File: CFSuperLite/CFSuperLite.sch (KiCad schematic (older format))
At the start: 23 parts, among them J1 IDE_CONNECTOR, J2 CF Adapter Power, J3 Bus_ISA_8bit, SW1 Options, U1 BIOS FLASH, U2 74HCT245, U3 ATF/GAL16V8x-15, U4 DS1315, Y1 32.768 KHz

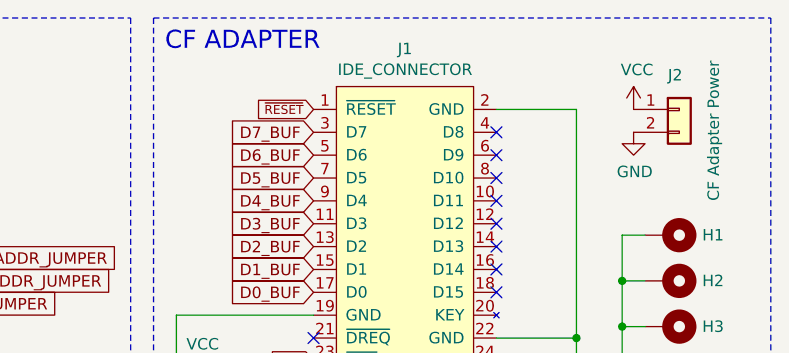
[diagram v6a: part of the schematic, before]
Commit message: CFSuperLite: Add diagram describing how the tall header with long pins should be fitted to the board.
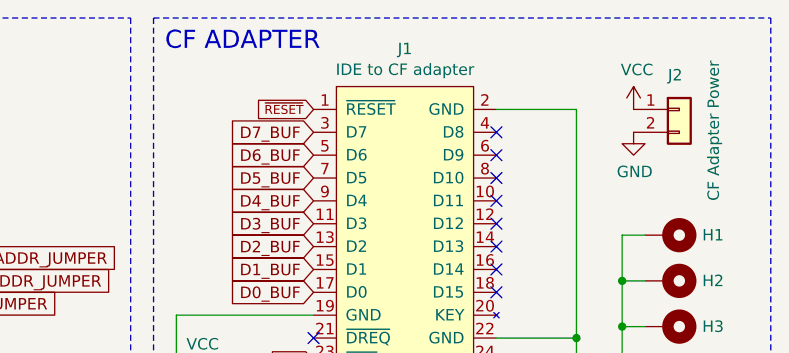
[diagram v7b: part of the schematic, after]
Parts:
- J1: value IDE_CONNECTOR -> IDE to CF adapter
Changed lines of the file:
@@
 P 9550 850
 F 0 "J1" H 9550 1015 50  0000 C CNN
-F 1 "IDE_CONNECTOR" H 9550 924 50  0000 C CNN
+F 1 "IDE to CF adapter" H 9550 924 50  0000 C CNN
 F 2 "Connector_PinSocket_2.54mm:PinSocket_2x20_P2.54mm_Vertical" H 9550 850 50  0001 C CNN
 F 3 "" H 9550 850 50  0001 C CNN

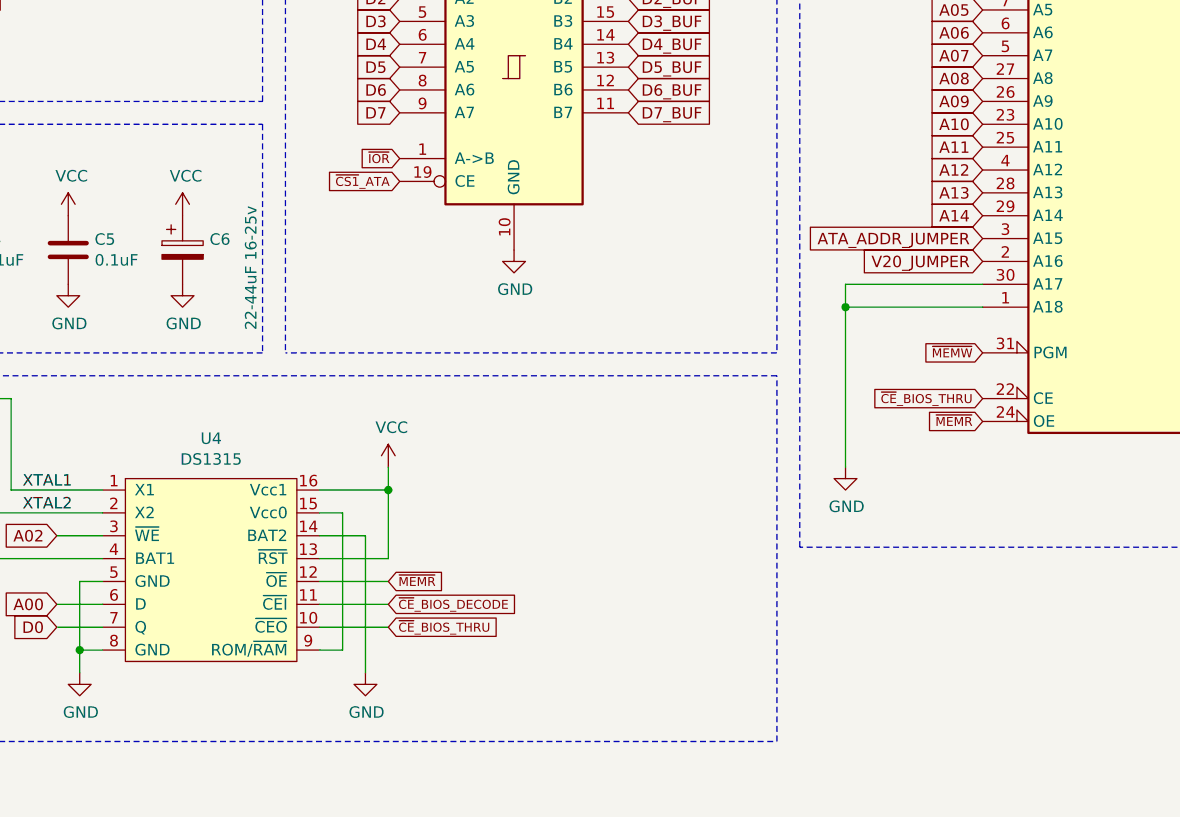
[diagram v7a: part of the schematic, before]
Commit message: CFSuperLite: Switch one tantalum to two smaller ones which are part of JLCPCB's basic part library.
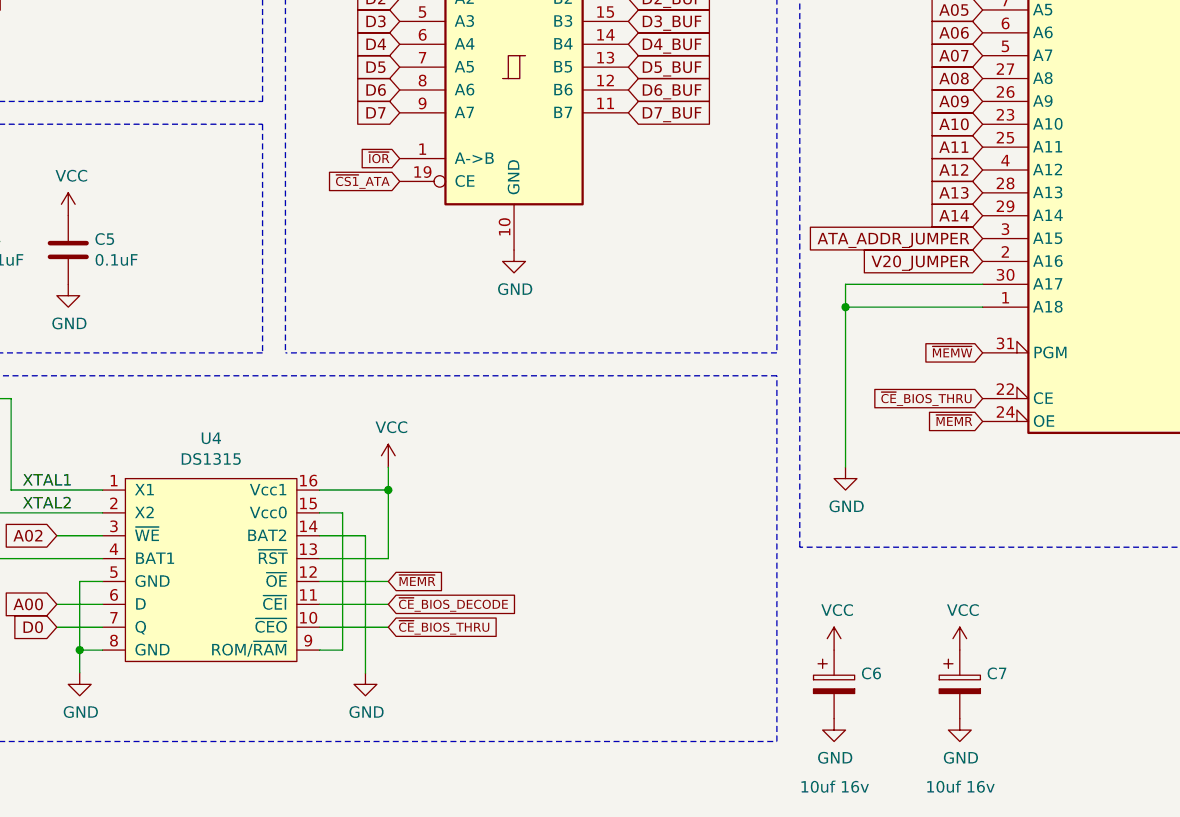
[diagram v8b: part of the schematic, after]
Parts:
- added C7: 10uf 16v, Capacitor_Tantalum_SMD:CP_EIA-3216-18_Kemet-A, symbol Device:CP
- C6: value 22-44uF 16-25v -> 10uf 16v; footprint Capacitor_Tantalum_SMD:CP_EIA-3528-15_AVX-H -> Capacitor_Tantalum_SMD:CP_EIA-3216-18_Kemet-A; LCSC C10785 -> C7171; Part options C10785, C125779, C139576 -> (none)
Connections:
- net GND: now also C7.2
- net VCC: now also C7.1
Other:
- moved on the sheet: C6
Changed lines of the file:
@@
 L Device:CP C6
 U 1 1 60440B68
-P 3200 5150
-F 0 "C6" H 3318 5196 50  0000 L CNN
-F 1 "22-44uF 16-25v" V 3500 4800 50  0000 L CNN
-F 2 "Capacitor_Tantalum_SMD:CP_EIA-3528-15_AVX-H" H 3238 5000 50  0001 C CNN
-F 3 "~" H 3200 5150 50  0001 C CNN
-F 4 "C10785" H 3200 5150 50  0001 C CNN "LCSC"
-F 5 "C10785, C125779,  C139576" H 3200 5150 50  0001 C CNN "Part options"
-	1    3200 5150
+P 6050 7050
+F 0 "C6" H 6168 7096 50  0000 L CNN
+F 1 "10uf 16v" H 5900 6600 50  0000 L CNN
+F 2 "Capacitor_Tantalum_SMD:CP_EIA-3216-18_Kemet-A" H 6088 6900 50  0001 C CNN
+F 3 "~" H 6050 7050 50  0001 C CNN
+F 4 "C7171" H 6050 7050 50  0001 C CNN "LCSC"
+F 5 "" H 6050 7050 50  0001 C CNN "Part options"
+	1    6050 7050
 	1    0    0    -1
 $EndComp
@@
 L power:GND #PWR0141
 U 1 1 6127AFFE
-P 3200 5300
-F 0 "#PWR0141" H 3200 5050 50  0001 C CNN
-F 1 "GND" H 3205 5127 50  0000 C CNN
-F 2 "" H 3200 5300 50  0001 C CNN
-F 3 "" H 3200 5300 50  0001 C CNN
-	1    3200 5300
+P 6050 7200
+F 0 "#PWR0141" H 6050 6950 50  0001 C CNN
+F 1 "GND" H 6055 7027 50  0000 C CNN
+F 2 "" H 6050 7200 50  0001 C CNN
+F 3 "" H 6050 7200 50  0001 C CNN
+	1    6050 7200
 	1    0    0    -1
 $EndComp
@@
 L power:VCC #PWR0140
 U 1 1 6127AA7C
-P 3200 5000
-F 0 "#PWR0140" H 3200 4850 50  0001 C CNN
-F 1 "VCC" H 3215 5173 50  0000 C CNN
-F 2 "" H 3200 5000 50  0001 C CNN
-F 3 "" H 3200 5000 50  0001 C CNN
-	1    3200 5000
+P 6050 6900
+F 0 "#PWR0140" H 6050 6750 50  0001 C CNN
+F 1 "VCC" H 6065 7073 50  0000 C CNN
+F 2 "" H 6050 6900 50  0001 C CNN
+F 3 "" H 6050 6900 50  0001 C CNN
+	1    6050 6900
 	1    0    0    -1
 $EndComp
@@
 Text GLabel 4950 1900 2    50   Input ~ 0
 A17
+$Comp
+L power:GND #PWR?
+U 1 1 6161E5C8
+P 6600 7200
+F 0 "#PWR?" H 6600 6950 50  0001 C CNN
+F 1 "GND" H 6605 7027 50  0000 C CNN
+F 2 "" H 6600 7200 50  0001 C CNN
+F 3 "" H 6600 7200 50  0001 C CNN
+	1    6600 7200
+	1    0    0    -1
+$EndComp
+$Comp
+L power:VCC #PWR?
+U 1 1 6161E5D2
+P 6600 6900
+F 0 "#PWR?" H 6600 6750 50  0001 C CNN
+F 1 "VCC" H 6615 7073 50  0000 C CNN
+F 2 "" H 6600 6900 50  0001 C CNN
+F 3 "" H 6600 6900 50  0001 C CNN
+	1    6600 6900
+	1    0    0    -1
+$EndComp
+$Comp
+L Device:CP C7
+U 1 1 616234E6
+P 6600 7050
+F 0 "C7" H 6718 7096 50  0000 L CNN
+F 1 "10uf 16v" H 6450 6600 50  0000 L CNN
+F 2 "Capacitor_Tantalum_SMD:CP_EIA-3216-18_Kemet-A" H 6638 6900 50  0001 C CNN
+F 3 "~" H 6600 7050 50  0001 C CNN
+F 4 "C7171" H 6600 7050 50  0001 C CNN "LCSC"
+F 5 "" H 6600 7050 50  0001 C CNN "Part options"
+	1    6600 7050
+	1    0    0    -1
+$EndComp
 $EndSCHEMATC
